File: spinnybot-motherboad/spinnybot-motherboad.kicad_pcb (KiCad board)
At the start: 2 copper layers, 63.5 x 63.5 mm, 52 parts, among them J1 LEDSTRIP1_CONN, J10 M2_GND, J11 M3_12V, J12 M3_GND, J13 GND, J14 M2_12V, J15 M3_SERIAL_CONN, J16 M2_SERIAL_CONN, J17 M1_SERIAL_CONN, J2 LEDSTRIP2_CONN, J3 LEDSTRIP3_CONN, J4 XBEE RESET, J5 XBEE FTDI, J6 CAP SWITCH, J7 +12V, J8 M1_12V, J9 M1_GND, Q1 SISA96DN, U1 SN74AHCT541N, U2 LM1117-5.0, U3 LM1117-3.3, U4 SN74LVC1G74, U5 XBP9B-DMWT-002

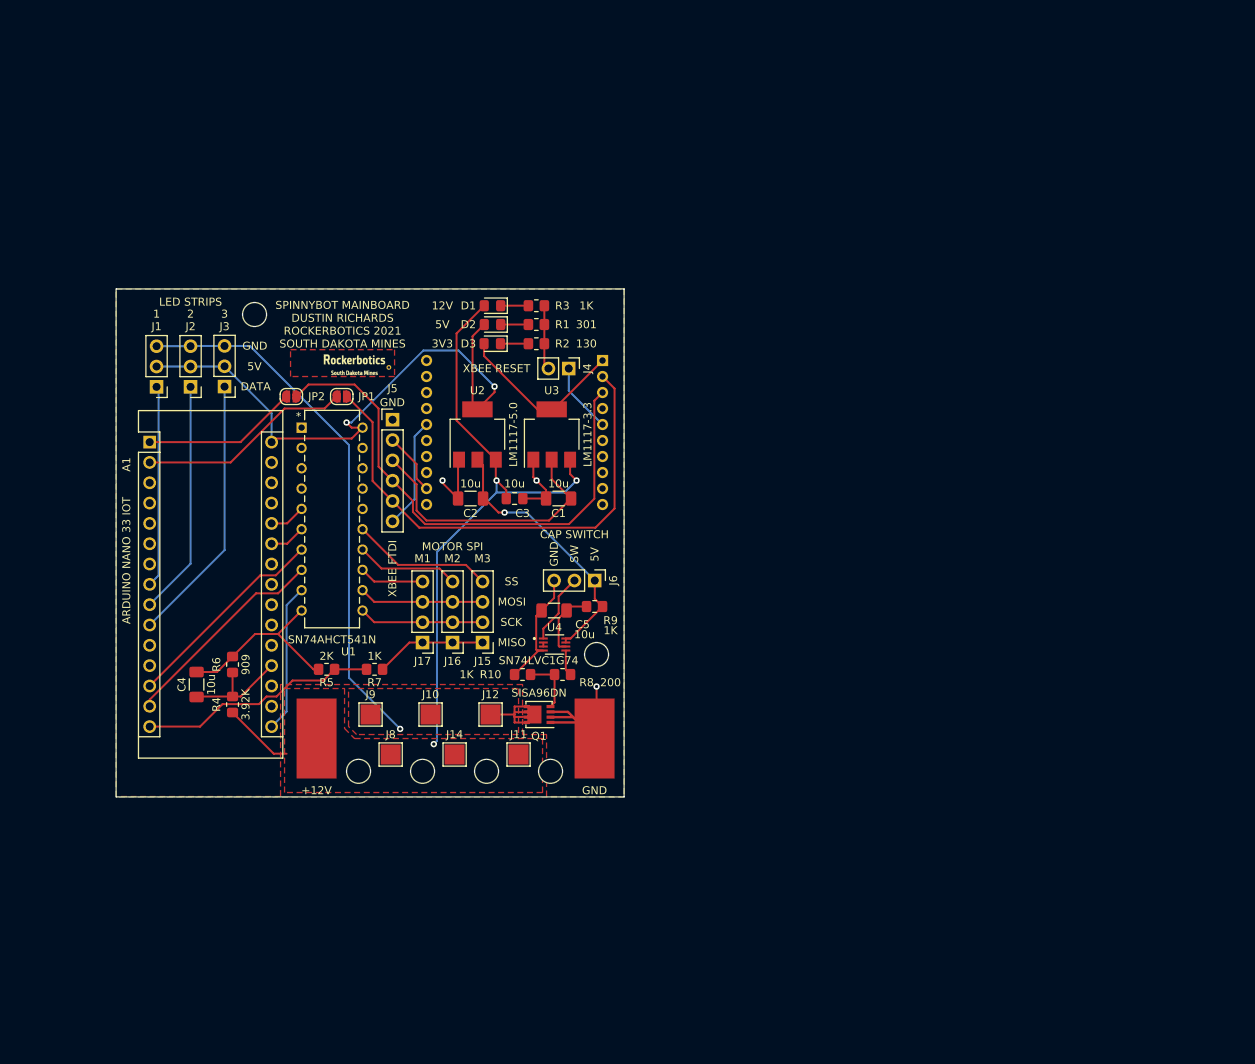
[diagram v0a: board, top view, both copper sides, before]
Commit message: board rev 2, got all components placed. still need to route
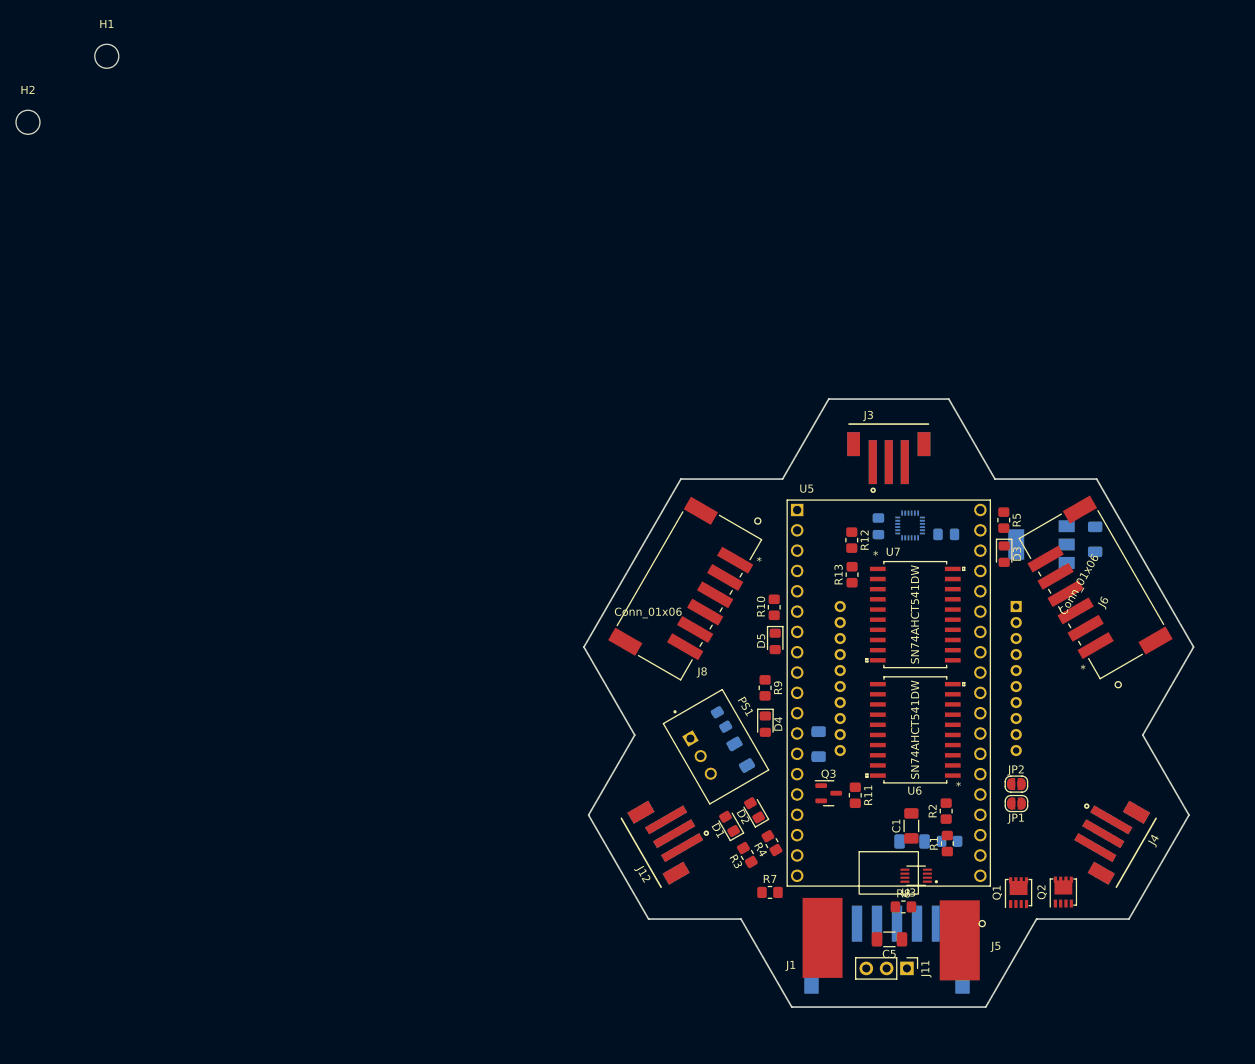
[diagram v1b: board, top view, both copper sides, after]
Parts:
- removed A1: ARDUINO NANO 33 IOT, Module:Arduino_Nano
- removed H3, H4, H6: PowerWire_Tiedown, MountingHole:MountingHole_3mm
- removed H5: SWITCH_TIEDOWN, MountingHole:MountingHole_3mm
- removed J10: M2_GND, TestPoint:TestPoint_Pad_2.5x2.5mm
- removed J15: M3_SERIAL_CONN, Connector_PinHeader_2.54mm:PinHeader_1x04_P2.54mm_Vertical
- removed J16: M2_SERIAL_CONN, Connector_PinHeader_2.54mm:PinHeader_1x04_P2.54mm_Vertical
- removed J17: M1_SERIAL_CONN, Connector_PinHeader_2.54mm:PinHeader_1x04_P2.54mm_Vertical
- removed J9: M1_GND, TestPoint:TestPoint_Pad_2.5x2.5mm
- removed TP2: LOGO2, robologo-shenzen:F.SilkS_g1611
- added C6: 10u, Capacitor_SMD:C_1206_3216Metric_Pad1.33x1.80mm_HandSolder, B.Cu at (175.7, 119.9)
- added C7: 0.1u, Capacitor_SMD:C_0805_2012Metric_Pad1.18x1.45mm_HandSolder, B.Cu at (171.5, 80.5)
- added C8: 0.1u, Capacitor_SMD:C_0805_2012Metric_Pad1.18x1.45mm_HandSolder, B.Cu at (180.0, 81.5)
- added C9: 10u, Capacitor_SMD:C_1206_3216Metric_Pad1.33x1.80mm_HandSolder, B.Cu at (164.0, 107.7)
- added D4: MOTOR_ACTIVE, LED_SMD:LED_0805_2012Metric_Pad1.15x1.40mm_HandSolder, F.Cu at (157.3, 105.2)
- added D5: STATUS, LED_SMD:LED_0805_2012Metric_Pad1.15x1.40mm_HandSolder, F.Cu at (158.6, 94.9)
- added PS1: R-78E5.0-1.0, R-78E5:CONV_R-78E5.0-1.0, F.Cu at (151.2, 108.1)
- added Q2: SISA96DN, Package_SO:Vishay_PowerPAK_1212-8_Single, F.Cu at (194.6, 126.2)
- added Q3: BC846, Package_TO_SOT_SMD:SOT-23, F.Cu at (165.3, 113.8)
- added R11: 1K, Resistor_SMD:R_0805_2012Metric_Pad1.20x1.40mm_HandSolder, F.Cu at (168.6, 114.1)
- added R12: 1K, Resistor_SMD:R_0805_2012Metric_Pad1.20x1.40mm_HandSolder, F.Cu at (168.2, 82.2)
- added R13: 2K, Resistor_SMD:R_0805_2012Metric_Pad1.20x1.40mm_HandSolder, F.Cu at (168.2, 86.5)
- added U6: SN74AHCT541DW, SN74AHCT541DW:SN74AHCT541DW, F.Cu at (176.1, 105.9)
- added U7: SN74AHCT541DW, SN74AHCT541DW:SN74AHCT541DW, F.Cu at (176.1, 91.5)
- C2: footprint Capacitor_SMD:C_1206_3216Metric_Pad1.33x1.80mm_HandSolder -> Capacitor_SMD:C_0805_2012Metric_Pad1.18x1.45mm_HandSolder; moved to B.Cu
- C3: footprint Capacitor_SMD:C_0805_2012Metric_Pad1.18x1.45mm_HandSolder -> Capacitor_SMD:C_1206_3216Metric_Pad1.33x1.80mm_HandSolder; moved to B.Cu
- C4: moved to B.Cu
- H2: value PowerWire_Tiedown -> SWITCH_TIEDOWN
- J1: value LEDSTRIP1_CONN -> +12V; footprint Connector_PinHeader_2.54mm:PinHeader_1x03_P2.54mm_Vertical -> Connector_Wire:SolderWirePad_1x01_SMD_5x10mm
- J11: value M3_12V -> CAP SWITCH; footprint TestPoint:TestPoint_Pad_2.5x2.5mm -> Connector_PinHeader_2.54mm:PinHeader_1x03_P2.54mm_Vertical
- J12: value M3_GND -> LEDSTRIP3_CONN1; footprint TestPoint:TestPoint_Pad_2.5x2.5mm -> B3B-PH-SM4:JST_B3B-PH-SM4-TB(LF)(SN)
- J13: value GND -> LEDSTRIP2_CONN2; footprint Connector_Wire:SolderWirePad_1x01_SMD_5x10mm -> B3B-PH-SM4:JST_B3B-PH-SM4-TB(LF)(SN); moved to B.Cu
- J14: value M2_12V -> LEDSTRIP3_CONN2; footprint TestPoint:TestPoint_Pad_2.5x2.5mm -> B3B-PH-SM4:JST_B3B-PH-SM4-TB(LF)(SN); moved to B.Cu
- J2: value LEDSTRIP2_CONN -> LEDSTRIP1_CONN2; footprint Connector_PinHeader_2.54mm:PinHeader_1x03_P2.54mm_Vertical -> B3B-PH-SM4:JST_B3B-PH-SM4-TB(LF)(SN); moved to B.Cu
- J3: value LEDSTRIP3_CONN -> LEDSTRIP1_CONN1; footprint Connector_PinHeader_2.54mm:PinHeader_1x03_P2.54mm_Vertical -> B3B-PH-SM4:JST_B3B-PH-SM4-TB(LF)(SN)
- J4: value XBEE RESET -> LEDSTRIP2_CONN1; footprint Connector_PinHeader_2.54mm:PinHeader_1x02_P2.54mm_Vertical -> B3B-PH-SM4:JST_B3B-PH-SM4-TB(LF)(SN)
- J5: value XBEE FTDI -> GND; footprint Connector_PinHeader_2.54mm:PinHeader_1x06_P2.54mm_Vertical -> Connector_Wire:SolderWirePad_1x01_SMD_5x10mm
- J6: value CAP SWITCH -> Conn_01x06; footprint Connector_PinHeader_2.54mm:PinHeader_1x03_P2.54mm_Vertical -> S6B-XH-SM4-TB:S6B-XH-SM4-TBLFSN
- J7: value +12V -> Conn_01x06; footprint Connector_Wire:SolderWirePad_1x01_SMD_5x10mm -> S6B-XH-SM4-TB:S6B-XH-SM4-TBLFSN; moved to B.Cu
- J8: value M1_12V -> Conn_01x06; footprint TestPoint:TestPoint_Pad_2.5x2.5mm -> S6B-XH-SM4-TB:S6B-XH-SM4-TBLFSN
- R1: value 301 -> 3.92K
- R10: value 1K -> 130
- R2: value 130 -> 909
- R4: value 3.92K -> 301
- R5: value 2K -> 130
- R6: value 909 -> 1K; moved to B.Cu
- R7: value 1K -> 10K
- U1: value SN74AHCT541N -> LM1117-3.3; footprint SN74AHCT541N:SN74AHCT541N -> Package_TO_SOT_SMD:SOT-223-3_TabPin2; moved to B.Cu
- U2: value LM1117-5.0 -> XBP9B-DMWT-002; footprint Package_TO_SOT_SMD:SOT-223-3_TabPin2 -> XBee_PRO900HP_S3B:DIP2200W51P200L3294H279Q20P; moved to B.Cu
- U3: value LM1117-3.3 -> SN74LVC1G74; footprint Package_TO_SOT_SMD:SOT-223-3_TabPin2 -> SN74LVC1G74DCUR:SOP50P310X90-8N
- U4: value SN74LVC1G74 -> ICM-20649; footprint SN74LVC1G74DCUR:SOP50P310X90-8N -> icm-20649:QFN40P300X300X95-24N; moved to B.Cu
- U5: value XBP9B-DMWT-002 -> ESP32-DEVKITC-32D; footprint XBee_PRO900HP_S3B:DIP2200W51P200L3294H279Q20P -> NODEMCU_ESP32:MODULE_NODEMCU_ESP32; moved to F.Cu
- moved C4 113.8 mm to (198.6, 82.1)
- moved J1 108.1 mm to (164.5, 131.9), turned to 0 degrees
- moved JP2 102.8 mm to (188.7, 112.7)
- moved JP1 98.5 mm to (188.7, 115.1)
- moved J5 96.2 mm to (181.7, 132.2)
- moved U1 93.6 mm to (191.9, 82.8), turned to 180 degrees
- moved R6 92.3 mm to (180.4, 119.8), turned to 180 degrees
- moved H2 91.0 mm to (65.2, 30.0)
- moved J4 90.8 mm to (201.5, 120.0), turned to -120 degrees
- moved J2 87.6 mm to (172.8, 70.2)
- moved R5 86.7 mm to (187.2, 79.7), turned to -90 degrees
- moved J3 83.3 mm to (172.8, 70.2), turned to 0 degrees
- moved R1 82.8 mm to (180.1, 120.1), turned to 90 degrees
- moved R2 77.7 mm to (179.9, 116.1), turned to 90 degrees
- moved J7 76.1 mm to (172.6, 133.7)
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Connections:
- C1 pad 1: +3V3 -> /12V_SENSE
- C2 pad 1: +5V -> GND
- C2 pad 2: GND -> +12V
- C3 pad 1: GND -> +5V
- C3 pad 2: +12V -> GND
- C4 pad 1: /12V_SENSE -> +3V3
- C5 pad 1: /DFF_RESET -> +5V
- J1 pad 1: /LEDSTRIP1_DATA -> +12V
- J11 pad 1: +12V -> +5V
- J12 pad 1: /MOTOR_NEG -> /LEDSTRIP3_DATA_5V
- J13 pad 1: GND -> /LEDSTRIP2_DATA_5V
- J14 pad 1: +12V -> /LEDSTRIP3_DATA_5V
- J2 pad 1: /LEDSTRIP3_DATA -> /LEDSTRIP1_DATA_5V
- J2 pad 3: /MOTOR_NEG -> /LEDSTRIP_GND
- J3 pad 1: /LEDSTRIP2_DATA -> /LEDSTRIP1_DATA_5V
- J3 pad 3: /MOTOR_NEG -> /LEDSTRIP_GND
- J4 pad 1: /XBEE_RESET -> /LEDSTRIP2_DATA_5V
- J4 pad 2: GND -> +5V
- J6 pad 1: +5V -> +12V
- J6 pad 2: /SWITCH -> /MOTOR_NEG
- J6 pad 3: GND -> /MISO_5V
- JP1 pad 1: /XBEE_TX -> /XBEE_RX
- JP1 pad 2: Net-(A1-Pad2) -> Net-(JP1-Pad2)
- JP2 pad 1: Net-(A1-Pad1) -> Net-(JP2-Pad1)
- JP2 pad 2: /XBEE_RX -> /XBEE_TX
- Q1 pad 5: /MOTOR_NEG -> /LEDSTRIP_GND
- R1 pad 1: Net-(D2-Pad1) -> +12V
- R1 pad 2: GND -> /12V_SENSE
- R10 pad 2: /FET_G -> Net-(D5-Pad1)
- R2 pad 1: Net-(D3-Pad1) -> /12V_SENSE
- R3 pad 1: Net-(D1-Pad1) -> GND
- R3 pad 2: GND -> Net-(D1-Pad1)
- R4 pad 1: +12V -> GND
- R4 pad 2: /12V_SENSE -> Net-(D2-Pad1)
- R5 pad 1: /MISO_3V3 -> GND
- R5 pad 2: GND -> Net-(D3-Pad1)
- R6 pad 1: /12V_SENSE -> +5V
- R6 pad 2: GND -> /DFF_RESET
- R7 pad 1: /MISO_5V -> GND
- R7 pad 2: /MISO_3V3 -> /FET_G
- R9 pad 1: +5V -> GND
- R9 pad 2: /DFF_RESET -> Net-(D4-Pad1)
- U1 pad 2: unconnected-(U1-Pad2) -> +3V3
- U1 pad 3: unconnected-(U1-Pad3) -> +5V
- U2 pad 1: GND -> +3V3
- U2 pad 2: +5V -> /XBEE_TX
- U2 pad 3: +12V -> /XBEE_RX
- U3 pad 1: GND -> /SWITCH
- U3 pad 2: +3V3 -> /DFF_QN
- U3 pad 3: +12V -> /DFF_QN
- U4 pad 1: /SWITCH -> (no net)
- U4 pad 2: /D_QN -> (no net)
- U4 pad 3: /D_QN -> (no net)
- U4 pad 4: GND -> (no net)
- U4 pad 5: /DFF_Q -> (no net)
- U4 pad 6: /DFF_RESET -> (no net)
- U4 pad 7: +5V -> unconnected-(U4-Pad7)
- U4 pad 8: +5V -> +3V3
- U5 pad 1: +3V3 -> unconnected-(U5-Pad1)
- U5 pad 10: GND -> /MCU and Buffers/LEDSTRIP2_DATA_3V3
- U5 pad 11: unconnected-(U5-Pad11) -> /MCU and Buffers/LEDSTRIP3_DATA_3V3
- U5 pad 12: /CTS# -> unconnected-(U5-Pad12)
- U5 pad 14: unconnected-(U5-Pad14) -> GND
- U5 pad 16: /RTS# -> unconnected-(U5-Pad16)
- U5 pad 19: unconnected-(U5-Pad19) -> +5V
- U5 pad 2: /XBEE_TX -> unconnected-(U5-Pad2)
- U5 pad 20: unconnected-(U5-Pad20) -> GND
- U5 pad 3: /XBEE_RX -> unconnected-(U5-Pad3)
- U5 pad 5: /XBEE_RESET -> unconnected-(U5-Pad5)
- U5 pad 8: (no net) -> Net-(D5-Pad2)
- U5 pad 9: unconnected-(U5-Pad9) -> /MCU and Buffers/LEDSTRIP1_DATA_3V3
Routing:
- net +5V: track 106.1 -> 0.00 mm, vias 3 -> 0
- net +12V: track 86.7 -> 0.00 mm, vias 3 -> 0
- net GND: track 84.7 -> 0.00 mm, vias 3 -> 0
- net /MOTOR_NEG: track 76.7 -> 0.00 mm, vias 1 -> 0
- net /XBEE_RX: track 65.1 -> 0.00 mm
- net /XBEE_TX: track 62.7 -> 0.00 mm
- net +3V3: track 55.7 -> 0.00 mm
- net /LEDSTRIP2_DATA: track 33.7 -> 0.00 mm
- net /MISO_3V3: track 30.1 -> 0.00 mm
- net /LEDSTRIP3_DATA: track 29.3 -> 0.00 mm
- net Net-(A1-Pad2): track 26.8 -> 0.00 mm
- net /MOSI_3V3: track 26.5 -> 0.00 mm
- net /CS1_3V3: track 26.1 -> 0.00 mm
- net /LEDSTRIP1_DATA: track 24.9 -> 0.00 mm
- net Net-(A1-Pad1): track 19.4 -> 0.00 mm
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- removed copper zone on F.Cu, net (none)
- removed copper zone on F.Cu, net +12V
- removed copper zone on F.Cu, net /MOTOR_NEG
- removed copper zone on B.Cu, net GND
- removed copper zone on F.Cu, net GND
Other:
- board size 63.5 x 63.5 mm -> 76.2 x 76 mm
- board text removed: "1"
- board text removed: "2"
- board text removed: "3"
- board text removed: "5V"
- board text removed: "DATA"
- board text removed: "GND"
- board text removed: "LED STRIPS"
- board text removed: "M1"
- board text removed: "M2"
- board text removed: "M3"
- board text removed: "MISO"
- board text removed: "MOSI"
- board text removed: "MOTOR SPI"
- board text removed: "NOT ALL WHO SPIN ARE LOST"
- board text removed: "SAMUEL {dblquote}JANITOR DUCK{dblquote} RYCKMAN ALEX {dblquote}GRON-GRON{dblquote} GRONLUND DUSTIN RICHARDS JOSEPH ALLEN PRATIK SINAI-KUNKOLIENKER LANDON LAMOREAUX"
- board text removed: "SCK"
- board text removed: "SPINNYBOT MAINBOARD DUSTIN RICHARDS ROCKERBOTICS 2021 SOUTH DAKOTA MINES"
- board text removed: "SS"
- board text removed: "SW"

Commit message: routed rev2 mainboard
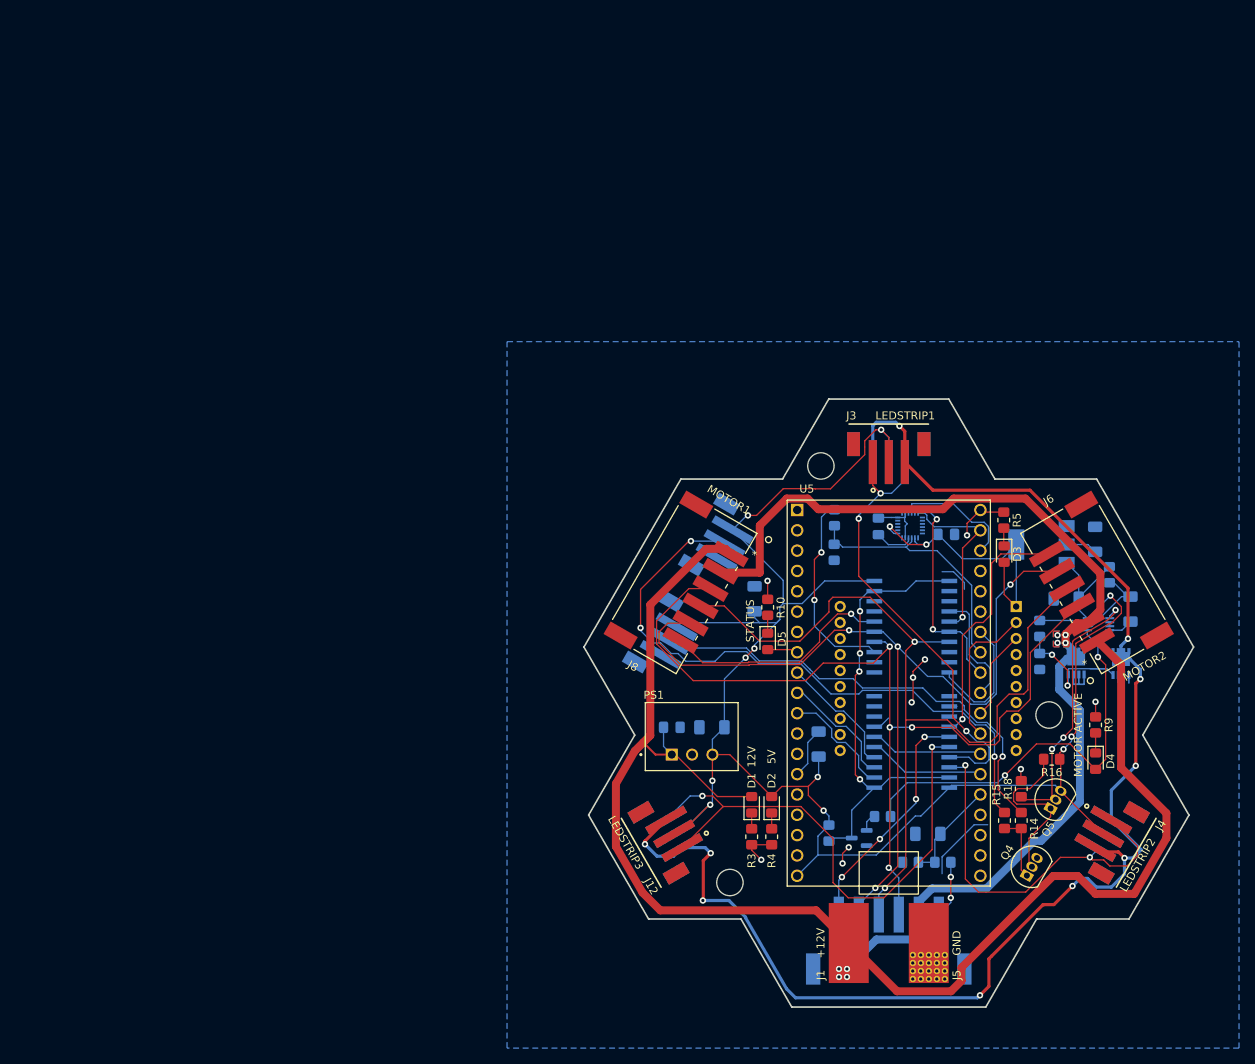
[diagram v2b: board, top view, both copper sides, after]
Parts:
- removed H2: SWITCH_TIEDOWN, MountingHole:MountingHole_3mm
- removed JP1, JP2: SolderJumper_2_Bridged, Jumper:SolderJumper-2_P1.3mm_Open_RoundedPad1.0x1.5mm
- removed TP1: LOGO1, robologo-shenzen:F.Mask_g1609
- added C10: 10u, Capacitor_SMD:C_1206_3216Metric_Pad1.33x1.80mm_HandSolder, B.Cu at (156.0, 89.5)
- added H3: MOUNTINGHOLE2, custom:MountingHole_3.3mm, F.Cu at (164.3, 72.9)
- added H4: MOUNTINGHOLE3, custom:MountingHole_3.3mm, F.Cu at (192.8, 104.1)
- added J9: CAP SWITCH, B3B-PH-SM4:JST_B3B-PH-SM4-TB(LF)(SN), B.Cu at (143.3, 93.6)
- added Q4: NPN, Package_TO_SOT_THT:TO-92_Inline, F.Cu at (190.0, 124.1)
- added Q5: PNP, Package_TO_SOT_THT:TO-92_Inline, F.Cu at (193.0, 115.7)
- added R14: 1K, Resistor_SMD:R_0805_2012Metric_Pad1.20x1.40mm_HandSolder, F.Cu at (189.3, 117.2)
- added R15: 1K, Resistor_SMD:R_0805_2012Metric_Pad1.20x1.40mm_HandSolder, F.Cu at (187.2, 117.2)
- added R16: 1K, Resistor_SMD:R_0805_2012Metric_Pad1.20x1.40mm_HandSolder, F.Cu at (193.1, 109.6)
- added R17: 10K, Resistor_SMD:R_0805_2012Metric_Pad1.20x1.40mm_HandSolder, B.Cu at (172.0, 116.8)
- added R18: 1K, Resistor_SMD:R_0805_2012Metric_Pad1.20x1.40mm_HandSolder, F.Cu at (189.3, 113.3)
- C1, C5, Q1, Q2, Q3, R1, R11, R12, R13, R2, R7, R8, U3, U6, U7: moved to B.Cu
- D4: value MOTOR_ACTIVE -> MOTOR ACTIVE
- H1: value LEDSTRIP_Tiedown -> MOUNTINGHOLE1; footprint MountingHole:MountingHole_3mm -> custom:MountingHole_3.3mm
- J11: footprint Connector_PinHeader_2.54mm:PinHeader_1x03_P2.54mm_Vertical -> B3B-PH-SM4:JST_B3B-PH-SM4-TB(LF)(SN); moved to B.Cu
- J12: value LEDSTRIP3_CONN1 -> LEDSTRIP3
- J13: value LEDSTRIP2_CONN2 -> LEDSTRIP2
- J14: value LEDSTRIP3_CONN2 -> LEDSTRIP3
- J2: value LEDSTRIP1_CONN2 -> LEDSTRIP1
- J3: value LEDSTRIP1_CONN1 -> LEDSTRIP1
- J4: value LEDSTRIP2_CONN1 -> LEDSTRIP2
- J5: footprint Connector_Wire:SolderWirePad_1x01_SMD_5x10mm -> custom:Stitched_SolderWirePad_1x01_SMD_5x10mm
- J6: value Conn_01x06 -> MOTOR2
- J7: value Conn_01x06 -> MOTOR3
- J8: value Conn_01x06 -> MOTOR1
- moved H1 129.4 mm to (152.9, 125.0)
- moved J11 59.6 mm to (150.3, 81.5), turned to -120 degrees
- moved C5 48.0 mm to (195.0, 89.5)
- moved R7 44.4 mm to (191.6, 97.4), turned to 90 degrees
- moved R9 41.6 mm to (198.6, 105.3)
- moved D4 41.5 mm to (198.6, 109.8)
- moved C6 39.9 mm to (203.0, 90.8), turned to -90 degrees
- moved R6 38.9 mm to (200.4, 86.5), turned to -90 degrees
- moved U3 38.8 mm to (199.0, 92.7)
- moved R8 38.8 mm to (191.6, 93.2), turned to 90 degrees
- moved Q1 31.4 mm to (201.8, 97.6)
- moved Q2 28.7 mm to (196.2, 97.6)
- moved U7 15.9 mm to (175.7, 107.4)
- moved U6 12.9 mm to (175.7, 93.0)
- moved R2 7.80 mm to (175.5, 122.5), turned to 180 degrees
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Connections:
- J11 pad 2: /SWITCH -> /SW2
- J6 pad 3: /MISO_5V -> /SCK_5V
- J6 pad 4: /SCK_5V -> /MISO_5V
- J6 pad 6: /MOTOR_CS3_5V -> /MOTOR_CS2_5V
- J7 pad 3: /MISO_5V -> /SCK_5V
- J7 pad 4: /SCK_5V -> /MISO_5V
- J7 pad 6: /MOTOR_CS2_5V -> /MOTOR_CS3_5V
- J7 pad 7: (no net) -> GND
- J8 pad 3: /MISO_5V -> /SCK_5V
- J8 pad 4: /SCK_5V -> /MISO_5V
- Q3 pad 1: /DFF_Q -> Net-(Q3-Pad1)
- U3 pad 1: /SWITCH -> /POWER_TOGGLE
- U5 pad 10: /MCU and Buffers/LEDSTRIP2_DATA_3V3 -> /MCU and Buffers/LEDSTRIP1_DATA_3V3
- U5 pad 11: /MCU and Buffers/LEDSTRIP3_DATA_3V3 -> /MCU and Buffers/LEDSTRIP2_DATA_3V3
- U5 pad 22: unconnected-(U5-Pad22) -> /MCU and Buffers/IMU_CS
- U5 pad 25: /MCU and Buffers/IMU_CS -> unconnected-(U5-Pad25)
- U5 pad 30: Net-(JP1-Pad2) -> /XBEE_RX
- U5 pad 31: Net-(JP2-Pad1) -> /XBEE_TX
- U5 pad 9: /MCU and Buffers/LEDSTRIP1_DATA_3V3 -> /MCU and Buffers/LEDSTRIP3_DATA_3V3
- U6 pad 17: /MOTOR_CS2_5V -> unconnected-(U6-Pad17)
- U6 pad 18: /MOTOR_CS3_5V -> unconnected-(U6-Pad18)
- U6 pad 2: /MCU and Buffers/MOTOR_CS3_3V3 -> GND
- U6 pad 3: /MCU and Buffers/MOTOR_CS2_3V3 -> GND
- U6 pad 8: unconnected-(U6-Pad8) -> GND
- U6 pad 9: unconnected-(U6-Pad9) -> GND
- U7 pad 14: unconnected-(U7-Pad14) -> /MOTOR_CS2_5V
- U7 pad 15: unconnected-(U7-Pad15) -> /MOTOR_CS3_5V
- U7 pad 17: /LEDSTRIP2_DATA_5V -> /LEDSTRIP1_DATA_5V
- U7 pad 18: /LEDSTRIP1_DATA_5V -> /LEDSTRIP2_DATA_5V
- U7 pad 2: /MCU and Buffers/LEDSTRIP1_DATA_3V3 -> /MCU and Buffers/LEDSTRIP2_DATA_3V3
- U7 pad 3: /MCU and Buffers/LEDSTRIP2_DATA_3V3 -> /MCU and Buffers/LEDSTRIP1_DATA_3V3
- U7 pad 5: unconnected-(U7-Pad5) -> /MCU and Buffers/MOTOR_CS3_3V3
- U7 pad 6: unconnected-(U7-Pad6) -> /MCU and Buffers/MOTOR_CS2_3V3
- U7 pad 7: unconnected-(U7-Pad7) -> GND
- U7 pad 8: unconnected-(U7-Pad8) -> GND
- U7 pad 9: unconnected-(U7-Pad9) -> GND
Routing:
- net +5V: track 0.00 -> 235.8 mm, vias 0 -> 11
- net +12V: track 0.00 -> 208.8 mm, vias 0 -> 6
- net /LEDSTRIP_GND: track 0.00 -> 182.8 mm, vias 0 -> 10
- net /MOTOR_NEG: track 0.00 -> 121.0 mm, vias 0 -> 4
- net /SCK_5V: track 0.00 -> 116.9 mm, vias 0 -> 4
- net /MOSI_5V: track 0.00 -> 111.7 mm, vias 0 -> 4
- net /MISO_5V: track 0.00 -> 110.3 mm, vias 0 -> 2
- net GND: track 0.00 -> 82.6 mm, vias 0 -> 10
- net /SW2: track 0.00 -> 79.6 mm, vias 0 -> 3
- net /LEDSTRIP3_DATA_5V: track 0.00 -> 67.7 mm, vias 0 -> 2
- net /SW1: track 0.00 -> 59.4 mm, vias 0 -> 1
- net /MCU and Buffers/BUFFER_OE: track 0.00 -> 57.6 mm, vias 0 -> 4
- net /LEDSTRIP1_DATA_5V: track 0.00 -> 57.4 mm, vias 0 -> 3
- net /DFF_Q: track 0.00 -> 57.3 mm, vias 0 -> 2
- net /LEDSTRIP2_DATA_5V: track 0.00 -> 48.6 mm, vias 0 -> 2
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- added copper zone on B.Cu, net /MOTOR_NEG
- added copper zone on F.Cu, net /MOTOR_NEG
- added copper zone on B.Cu, net GND
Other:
- board text added: "SPINNYBOT MOTHERBOARD REV2 DUSTIN RICHARDS ROCKERBOTICS 2021 SOUTH DAKOTA MINES"

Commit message: added graphics and generated gerbers
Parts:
- added G***: LOGO, robologo-shenzen-25mm:F.SilkS_g1611, B.Cu at (196.3, 111.2)
- added REF**: nofcc, robologo-shenzen-25mm:nofcc, B.Cu at (153.9, 97.2)
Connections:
- J7 pad 7: GND -> (no net)
- U2 pad 12: /CTS# -> unconnected-(U2-Pad12)
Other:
- board text added: "ALL I DO IS SPIN SPIN SPIN NO MATTER WHAT"
